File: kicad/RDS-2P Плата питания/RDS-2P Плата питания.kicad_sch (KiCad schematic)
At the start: 13 parts, among them J1 XT30U, J2 XT30U2, J3 ЗАР, J4 ВЫКЛ, J5 8.4V, J6 8.4V, J7 5V, J8 ИНД, U1 Converter_Mini560, U2 BMS_2S_20A

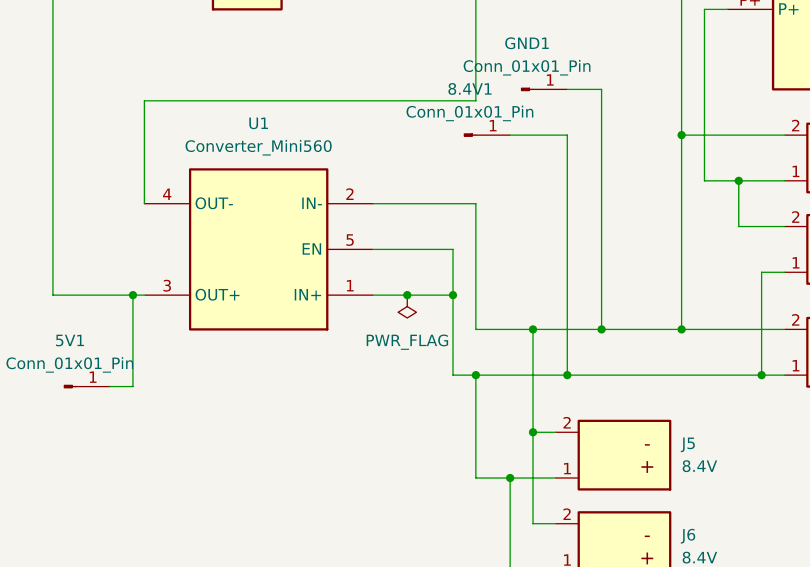
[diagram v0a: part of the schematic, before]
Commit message: Fix: pinout Mini560
Исправил распиновку Mini560 на платах
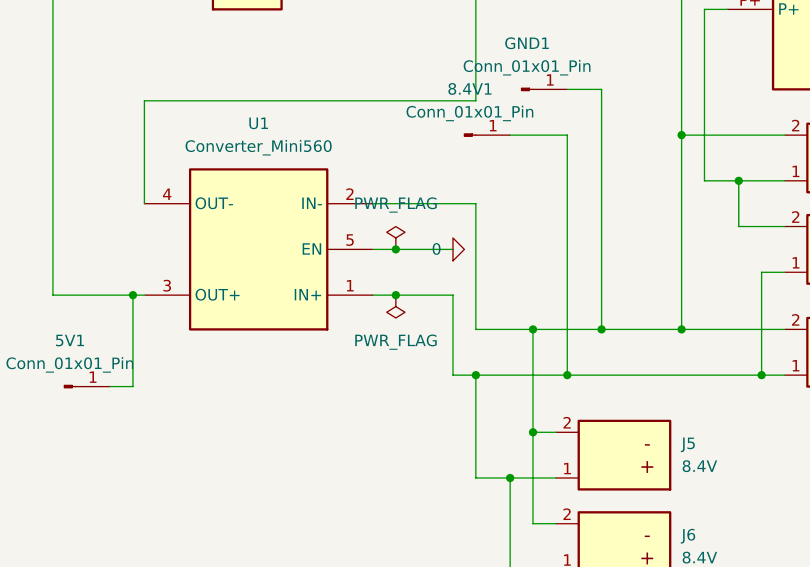
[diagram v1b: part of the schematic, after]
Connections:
- net at 8.4V1.1 (Pin_1), J4.1, J5.1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: no longer U1.5 (EN)
- new net 0: U1.5 (EN)
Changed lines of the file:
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@@
+	)
+	(junction
+		(at 101.6 113.03)
+		(diameter 0)
+		(color 0 0 0 0)
 	)
 	(junction
@@
 	)
 	(junction
-		(at 102.87 118.11)
-		(diameter 0)
-		(color 0 0 0 0)
-	)
-	(junction
 		(at 171.45 77.47)
 		(diameter 0)
@@
 	)
 	(junction
+		(at 101.6 118.11)
+		(diameter 0)
+		(color 0 0 0 0)
+	)
+	(junction
 		(at 173.99 85.09)
 		(diameter 0)
@@
 	)
 	(junction
-		(at 107.95 118.11)
-		(diameter 0)
-		(color 0 0 0 0)
-	)
-	(junction
 		(at 133.35 100.33)
 		(diameter 0)
@@
 	(wire
 		(pts
-			(xy 102.87 118.11) (xy 107.95 118.11)
-		)
-		(stroke
-			(width 0)
-			(type default)
-		)
-	)
-	(wire
-		(pts
-			(xy 107.95 118.11) (xy 107.95 127)
-		)
-		(stroke
-			(width 0)
-			(type default)
-		)
-	)
-	(wire
-		(pts
 			(xy 116.84 133.35) (xy 119.38 133.35)
 		)
@@
 	(wire
 		(pts
-			(xy 107.95 113.03) (xy 99.06 113.03)
+			(xy 107.95 113.03) (xy 101.6 113.03)
 		)
 		(stroke
@@
 	(wire
 		(pts
+			(xy 101.6 113.03) (xy 99.06 113.03)
+		)
+		(stroke
+			(width 0)
+			(type default)
+		)
+	)
+	(wire
+		(pts
 			(xy 110.49 121.92) (xy 116.84 121.92)
 		)
@@
 	(wire
 		(pts
+			(xy 107.95 127) (xy 107.95 118.11)
+		)
+		(stroke
+			(width 0)
+			(type default)
+		)
+	)
+	(wire
+		(pts
+			(xy 107.95 118.11) (xy 101.6 118.11)
+		)
+		(stroke
+			(width 0)
+			(type default)
+		)
+	)
+	(wire
+		(pts
 			(xy 99.06 107.95) (xy 110.49 107.95)
 		)
@@
 	(wire
 		(pts
-			(xy 107.95 118.11) (xy 107.95 113.03)
-		)
-		(stroke
-			(width 0)
-			(type default)
-		)
-	)
-	(wire
-		(pts
 			(xy 144.78 110.49) (xy 139.7 110.49)
 		)
@@
 	(wire
 		(pts
-			(xy 99.06 118.11) (xy 102.87 118.11)
-		)
-		(stroke
-			(width 0)
-			(type default)
-		)
-	)
-	(wire
-		(pts
 			(xy 72.39 128.27) (xy 72.39 118.11)
 		)
@@
 		(pts
 			(xy 110.49 138.43) (xy 114.3 138.43)
+		)
+		(stroke
+			(width 0)
+			(type default)
+		)
+	)
+	(wire
+		(pts
+			(xy 101.6 118.11) (xy 99.06 118.11)
 		)
 		(stroke
@@
 	(symbol
 		(lib_id "power:PWR_FLAG")
-		(at 102.87 118.11 180)
+		(at 101.6 118.11 180)
 		(unit 1)
 		(exclude_from_sim no)
@@
 		(fields_autoplaced yes)
 		(property "Reference" "#FLG04"
-			(at 102.87 120.015 0)
+			(at 101.6 120.015 0)
 			(effects
 				(font
@@
 		)
 		(property "Value" "PWR_FLAG"
-			(at 102.87 123.19 0)
+			(at 101.6 123.19 0)
 			(effects
 				(font
@@
 		)
 		(property "Footprint" ""
-			(at 102.87 118.11 0)
+			(at 101.6 118.11 0)
 			(effects
 				(font
@@
 		)
 		(property "Datasheet" "~"
-			(at 102.87 118.11 0)
+			(at 101.6 118.11 0)
 			(effects
 				(font
@@
 		)
 		(property "Description" "Special symbol for telling ERC where power comes from"
-			(at 102.87 118.11 0)
+			(at 101.6 118.11 0)
 			(effects
 				(font
@@
 	)
 	(symbol
+		(lib_id "power:PWR_FLAG")
+		(at 101.6 113.03 0)
+		(unit 1)
+		(exclude_from_sim no)
+		(in_bom yes)
+		(on_board yes)
+		(dnp no)
+		(fields_autoplaced yes)
+		(property "Reference" "#FLG05"
+			(at 101.6 111.125 0)
+			(effects
+				(font
+					(size 1.27 1.27)
+				)
+				(hide yes)
+			)
+		)
+		(property "Value" "PWR_FLAG"
+			(at 101.6 107.95 0)
+			(effects
+				(font
+					(size 1.27 1.27)
+				)
+			)
+		)
+		(property "Footprint" ""
+			(at 101.6 113.03 0)
+			(effects
+				(font
+					(size 1.27 1.27)
+				)
+				(hide yes)
+			)
+		)
+		(property "Datasheet" "~"
+			(at 101.6 113.03 0)
+			(effects
+				(font
+					(size 1.27 1.27)
+				)
+				(hide yes)
+			)
+		)
+		(property "Description" "Special symbol for telling ERC where power comes from"
+			(at 101.6 113.03 0)
+			(effects
+				(font
+					(size 1.27 1.27)
+				)
+				(hide yes)
+			)
+		)
+		(pin "1"
+		)
+		(instances
+			(project "RDS-2P Плата питания"
+				(path "/d5c9be49-5131-4716-b5ec-8d0e4e4e0be0"
+					(reference "#FLG05")
+					(unit 1)
+				)
+			)
+		)
+	)
+	(symbol
 		(lib_id "Amass_XT30U:XT30U")
 		(at 85.09 81.28 90)
@@
 					(unit 1)
 				)
+			)
+		)
+	)
+	(symbol
+		(lib_id "Simulation_SPICE:0")
+		(at 107.95 113.03 90)
+		(unit 1)
+		(exclude_from_sim no)
+		(in_bom yes)
+		(on_board yes)
+		(dnp no)
+		(fields_autoplaced yes)
+		(property "Reference" "#GND03"
+			(at 113.03 113.03 0)
+			(effects
+				(font
+					(size 1.27 1.27)
+				)
+				(hide yes)
+			)
+		)
+		(property "Value" "0"
+			(at 106.68 113.0299 90)
+			(effects
+				(font
+					(size 1.27 1.27)
+				)
+				(justify left)
+			)
+		)
+		(property "Footprint" ""
+			(at 107.95 113.03 0)
+			(effects
+				(font
+					(size 1.27 1.27)
+				)
+				(hide yes)
+			)
+		)
+		(property "Datasheet" "https://ngspice.sourceforge.io/docs/ngspice-html-manual/manual.xhtml#subsec_Circuit_elements__device"
+			(at 118.11 113.03 0)
+			(effects
+				(font
+					(size 1.27 1.27)
+				)
+				(hide yes)
+			)
+		)
+		(property "Description" "0V reference potential for simulation"
+			(at 115.57 113.03 0)
+			(effects
+				(font
+					(size 1.27 1.27)
+				)
+				(hide yes)
+			)
+		)
+		(pin "1"
+		)
+		(instances
+			(project ""
+				(path "/d5c9be49-5131-4716-b5ec-8d0e4e4e0be0"
+					(reference "#GND03")
+					(unit 1)
+				)
